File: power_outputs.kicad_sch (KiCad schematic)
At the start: 10 parts, among them Q1 BSS138, Q3 MMBT3904, Q4 MMBT3906

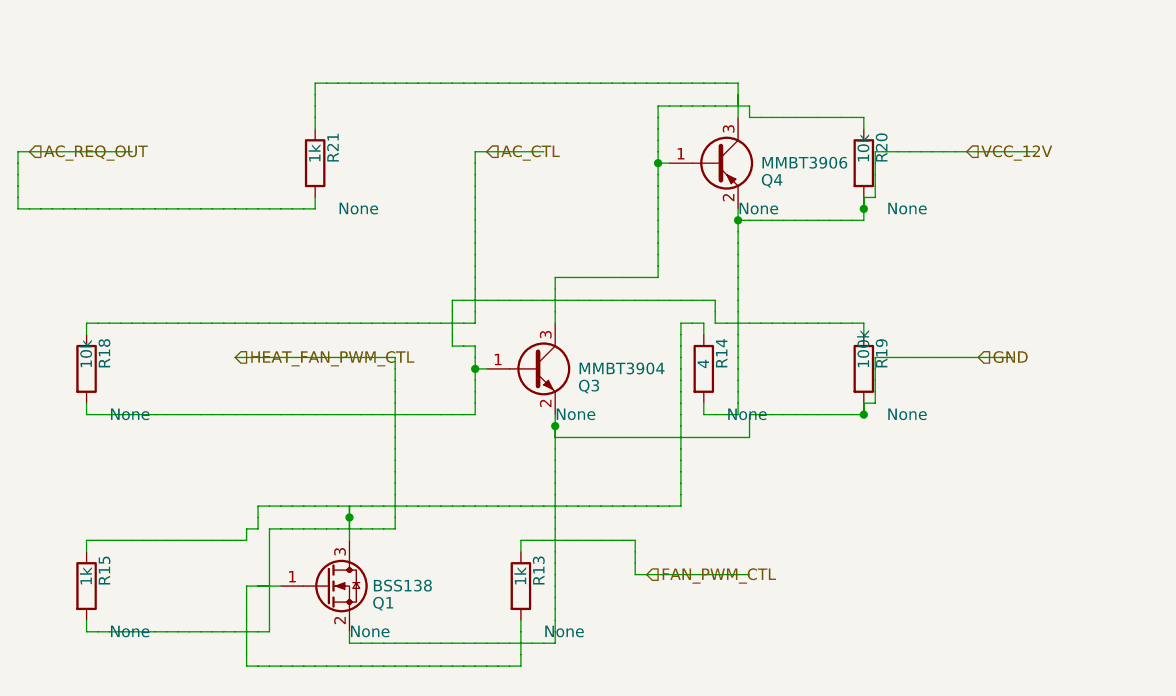
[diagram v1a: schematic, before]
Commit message: fix router map cell no more mark for pins
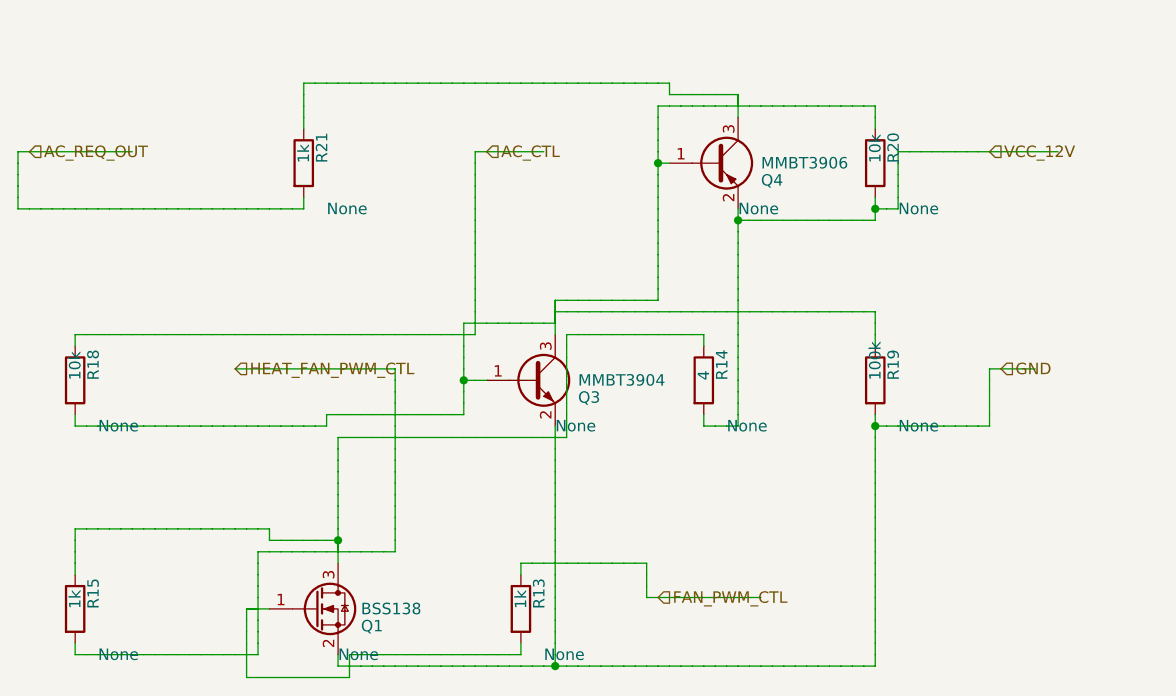
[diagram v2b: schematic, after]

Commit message: рефакторинг проекта и начала прогона тестов
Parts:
- R14: value 4 -> 4.7k

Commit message: fix writer
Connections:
- net AC_CTL: no longer Q1.1 (G), Q1.2 (S), Q1.3 (D), Q3.1 (B), Q3.2 (E), Q3.3 (C), Q4.1 (B), Q4.2 (E), Q4.3 (C), R13.1, R13.2, R14.1, R14.2, R15.1, R15.2, R18.2, R19.1, R19.2, R20.1, R20.2, R21.1
- new net: Q1.3 (D), R14.1, R15.1
- new net: Q3.1 (B), Q3.3 (C), Q4.1 (B), R18.2, R19.1, R20.1
- new net: Q4.3 (C), R21.1
- new net: Q1.1 (G), R13.2
- new net FAN_PWM_CTL: R13.1
- new net GND: Q1.2 (S), Q3.2 (E), R19.2
- new net HEAT_FAN_PWM_CTL: R15.2
- new net VCC_12V: Q4.2 (E), R14.2, R20.2

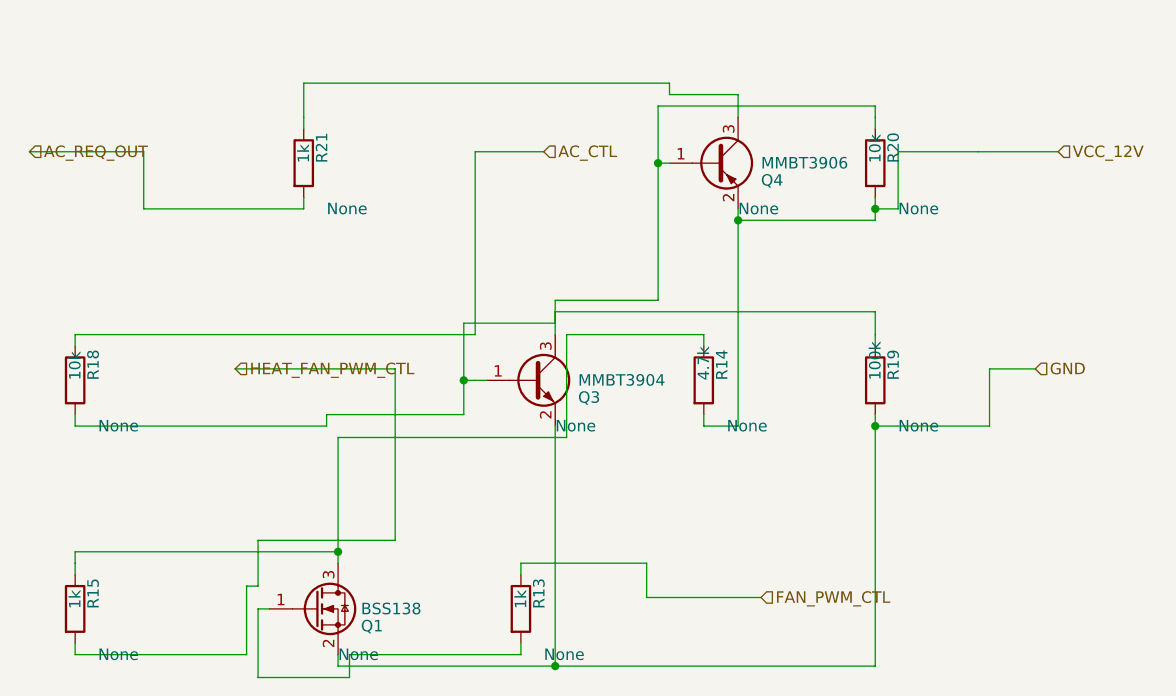
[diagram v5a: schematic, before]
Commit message: реализована 2я занятость клетки
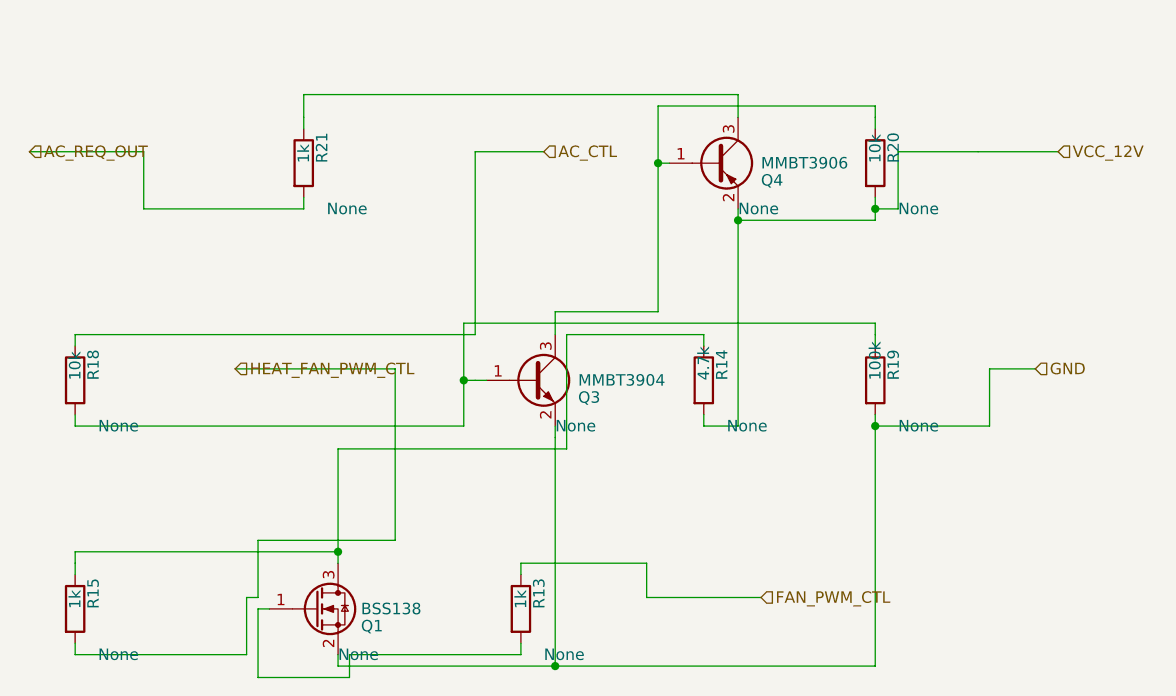
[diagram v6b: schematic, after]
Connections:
- net at Q3.1 (B), R18.2, R19.1: no longer Q3.3 (C), Q4.1 (B), R20.1
- new net: Q3.3 (C), Q4.1 (B), R20.1
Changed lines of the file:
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@@
 		(instances
 			(project "Untitled"
-				(path "/2bec01fa-02fa-473d-b0ad-ed352eecf5c4"
+				(path "/d529702e-f007-4e27-8b1f-a583131970cf"
 					(reference "Q1")
 					(unit 1)
@@
 		(instances
 			(project "Untitled"
-				(path "/2bec01fa-02fa-473d-b0ad-ed352eecf5c4"
+				(path "/d529702e-f007-4e27-8b1f-a583131970cf"
 					(reference "Q3")
 					(unit 1)
@@
 		(instances
 			(project "Untitled"
-				(path "/2bec01fa-02fa-473d-b0ad-ed352eecf5c4"
+				(path "/d529702e-f007-4e27-8b1f-a583131970cf"
 					(reference "Q4")
 					(unit 1)
@@
 		(instances
 			(project "Untitled"
-				(path "/2bec01fa-02fa-473d-b0ad-ed352eecf5c4"
+				(path "/d529702e-f007-4e27-8b1f-a583131970cf"
 					(reference "R13")
 					(unit 1)
@@
 		(instances
 			(project "Untitled"
-				(path "/2bec01fa-02fa-473d-b0ad-ed352eecf5c4"
+				(path "/d529702e-f007-4e27-8b1f-a583131970cf"
 					(reference "R14")
 					(unit 1)
@@
 		(instances
 			(project "Untitled"
-				(path "/2bec01fa-02fa-473d-b0ad-ed352eecf5c4"
+				(path "/d529702e-f007-4e27-8b1f-a583131970cf"
 					(reference "R15")
 					(unit 1)
@@
 		(instances
 			(project "Untitled"
-				(path "/2bec01fa-02fa-473d-b0ad-ed352eecf5c4"
+				(path "/d529702e-f007-4e27-8b1f-a583131970cf"
 					(reference "R18")
 					(unit 1)
@@
 		(instances
 			(project "Untitled"
-				(path "/2bec01fa-02fa-473d-b0ad-ed352eecf5c4"
+				(path "/d529702e-f007-4e27-8b1f-a583131970cf"
 					(reference "R19")
 					(unit 1)
@@
 		(instances
 			(project "Untitled"
-				(path "/2bec01fa-02fa-473d-b0ad-ed352eecf5c4"
+				(path "/d529702e-f007-4e27-8b1f-a583131970cf"
 					(reference "R20")
 					(unit 1)
@@
 		(instances
 			(project "Untitled"
-				(path "/2bec01fa-02fa-473d-b0ad-ed352eecf5c4"
+				(path "/d529702e-f007-4e27-8b1f-a583131970cf"
 					(reference "R21")
 					(unit 1)
@@
 	(wire
 		(pts
-			(xy 63.5 27.94) (xy 63.5 39.37)
-		)
-		(stroke
-			(width 0)
-			(type default)
-		)
-	)
-	(wire
-		(pts
-			(xy 63.5 39.37) (xy 38.1 39.37)
-		)
-		(stroke
-			(width 0)
-			(type default)
-		)
-	)
-	(wire
-		(pts
-			(xy 38.1 39.37) (xy 38.1 52.07)
+			(xy 63.5 27.94) (xy 63.5 40.64)
+		)
+		(stroke
+			(width 0)
+			(type default)
+		)
+	)
+	(wire
+		(pts
+			(xy 63.5 40.64) (xy 38.1 40.64)
+		)
+		(stroke
+			(width 0)
+			(type default)
+		)
+	)
+	(wire
+		(pts
+			(xy 38.1 40.64) (xy 38.1 52.07)
 		)
 		(stroke
@@
 	(wire
 		(pts
-			(xy 52.07 26.67) (xy 62.23 26.67)
-		)
-		(stroke
-			(width 0)
-			(type default)
-		)
-	)
-	(wire
-		(pts
-			(xy 62.23 26.67) (xy 62.23 25.4)
-		)
-		(stroke
-			(width 0)
-			(type default)
-		)
-	)
-	(wire
-		(pts
-			(xy 62.23 25.4) (xy 97.79 25.4)
-		)
-		(stroke
-			(width 0)
-			(type default)
-		)
-	)
-	(wire
-		(pts
-			(xy 97.79 25.4) (xy 97.79 27.94)
+			(xy 52.07 26.67) (xy 97.79 26.67)
+		)
+		(stroke
+			(width 0)
+			(type default)
+		)
+	)
+	(wire
+		(pts
+			(xy 97.79 26.67) (xy 97.79 27.94)
 		)
 		(stroke
@@
 	(wire
 		(pts
-			(xy 8.89 38.1) (xy 36.83 38.1)
-		)
-		(stroke
-			(width 0)
-			(type default)
-		)
-	)
-	(wire
-		(pts
-			(xy 36.83 38.1) (xy 36.83 36.83)
-		)
-		(stroke
-			(width 0)
-			(type default)
-		)
-	)
-	(wire
-		(pts
-			(xy 36.83 36.83) (xy 52.07 36.83)
-		)
-		(stroke
-			(width 0)
-			(type default)
-		)
-	)
-	(wire
-		(pts
-			(xy 52.07 36.83) (xy 52.07 33.02)
+			(xy 8.89 38.1) (xy 52.07 38.1)
+		)
+		(stroke
+			(width 0)
+			(type default)
+		)
+	)
+	(wire
+		(pts
+			(xy 52.07 38.1) (xy 52.07 33.02)
 		)
 		(stroke
@@
 	(wire
 		(pts
-			(xy 62.23 27.94) (xy 62.23 24.13)
-		)
-		(stroke
-			(width 0)
-			(type default)
-		)
-	)
-	(wire
-		(pts
-			(xy 62.23 24.13) (xy 73.66 24.13)
-		)
-		(stroke
-			(width 0)
-			(type default)
-		)
-	)
-	(wire
-		(pts
-			(xy 73.66 24.13) (xy 73.66 8.89)
+			(xy 62.23 27.94) (xy 62.23 25.4)
+		)
+		(stroke
+			(width 0)
+			(type default)
+		)
+	)
+	(wire
+		(pts
+			(xy 62.23 25.4) (xy 73.66 25.4)
+		)
+		(stroke
+			(width 0)
+			(type default)
+		)
+	)
+	(wire
+		(pts
+			(xy 73.66 25.4) (xy 73.66 8.89)
 		)
 		(stroke
@@
 	(wire
 		(pts
-			(xy 82.55 1.27) (xy 74.93 1.27)
-		)
-		(stroke
-			(width 0)
-			(type default)
-		)
-	)
-	(wire
-		(pts
-			(xy 74.93 1.27) (xy 74.93 0)
-		)
-		(stroke
-			(width 0)
-			(type default)
-		)
-	)
-	(wire
-		(pts
-			(xy 74.93 0) (xy 34.29 0)
-		)
-		(stroke
-			(width 0)
-			(type default)
-		)
-	)
-	(wire
-		(pts
-			(xy 34.29 0) (xy 34.29 3.81)
+			(xy 82.55 1.27) (xy 34.29 1.27)
+		)
+		(stroke
+			(width 0)
+			(type default)
+		)
+	)
+	(wire
+		(pts
+			(xy 34.29 1.27) (xy 34.29 3.81)
 		)
 		(stroke
@@
 	(wire
 		(pts
-			(xy 27.94 63.5) (xy 27.94 55.88)
-		)
-		(stroke
-			(width 0)
-			(type default)
-		)
-	)
-	(wire
-		(pts
-			(xy 27.94 55.88) (xy 29.21 55.88)
-		)
-		(stroke
-			(width 0)
-			(type default)
-		)
-	)
-	(wire
-		(pts
-			(xy 29.21 55.88) (xy 29.21 50.8)
-		)
-		(stroke
+			(xy 27.94 63.5) (xy 27.94 57.15)
+		)
+		(stroke
+			(width 0)
+			(type default)
+		)
+	)
+	(wire
+		(pts
+			(xy 27.94 57.15) (xy 29.21 57.15)
+		)
+		(stroke
+			(width 0)
+			(type default)
+		)
+	)
+	(wire
+		(pts
+			(xy 29.21 57.15) (xy 29.21 50.8)
+		)
+		(stroke

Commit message: fic placer for small schemes
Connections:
- net AC_BASE: now reaches Q3.1 (B), R18.2, R19.1
- net AC_PNP_BASE: now reaches Q3.3 (C), Q4.1 (B), R20.1
- net FAN_GATE: now reaches Q1.1 (G), R13.2
- net FAN_PWM_NODE: now reaches Q1.3 (D), R14.1, R15.1
- net AC_REQ: now reaches Q4.3 (C), R21.1
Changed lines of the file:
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@@
 		(instances
 			(project "Untitled"
-				(path "/445c904c-f531-4f41-953b-9ab8c092722a"
+				(path "/bd3444a0-416b-43f5-847d-17557aca00e5"
 					(reference "Q1")
 					(unit 1)
@@
 		(instances
 			(project "Untitled"
-				(path "/445c904c-f531-4f41-953b-9ab8c092722a"
+				(path "/bd3444a0-416b-43f5-847d-17557aca00e5"
 					(reference "Q3")
 					(unit 1)
@@
 		(instances
 			(project "Untitled"
-				(path "/445c904c-f531-4f41-953b-9ab8c092722a"
+				(path "/bd3444a0-416b-43f5-847d-17557aca00e5"
 					(reference "Q4")
 					(unit 1)
@@
 		(instances
 			(project "Untitled"
-				(path "/445c904c-f531-4f41-953b-9ab8c092722a"
+				(path "/bd3444a0-416b-43f5-847d-17557aca00e5"
 					(reference "R13")
 					(unit 1)
@@
 		(instances
 			(project "Untitled"
-				(path "/445c904c-f531-4f41-953b-9ab8c092722a"
+				(path "/bd3444a0-416b-43f5-847d-17557aca00e5"
 					(reference "R14")
 					(unit 1)
@@
 		(instances
 			(project "Untitled"
-				(path "/445c904c-f531-4f41-953b-9ab8c092722a"
+				(path "/bd3444a0-416b-43f5-847d-17557aca00e5"
 					(reference "R15")
 					(unit 1)
@@
 		(instances
 			(project "Untitled"
-				(path "/445c904c-f531-4f41-953b-9ab8c092722a"
+				(path "/bd3444a0-416b-43f5-847d-17557aca00e5"
 					(reference "R18")
 					(unit 1)
@@
 		(instances
 			(project "Untitled"
-				(path "/445c904c-f531-4f41-953b-9ab8c092722a"
+				(path "/bd3444a0-416b-43f5-847d-17557aca00e5"
 					(reference "R19")
 					(unit 1)
@@
 		(instances
 			(project "Untitled"
-				(path "/445c904c-f531-4f41-953b-9ab8c092722a"
+				(path "/bd3444a0-416b-43f5-847d-17557aca00e5"
 					(reference "R20")
 					(unit 1)
@@
 		(instances
 			(project "Untitled"
-				(path "/445c904c-f531-4f41-953b-9ab8c092722a"
+				(path "/bd3444a0-416b-43f5-847d-17557aca00e5"
 					(reference "R21")
 					(unit 1)
@@
 		(color 0 0 0 0)
 	)
+	(label "FAN_GATE"
+		(at 49.53 63.5 270)
+		(effects
+			(font
+				(size 1.27 1.27)
+			)
+			(justify left bottom)
+		)
+	)
+	(label "FAN_PWM_NODE"
+		(at 71.12 27.94 90)
+		(effects
+			(font
+				(size 1.27 1.27)
+			)
+			(justify left bottom)
+		)
+	)
+	(label "AC_BASE"
+		(at 53.34 33.02 180)
+		(effects
+			(font
+				(size 1.27 1.27)
+			)
+			(justify left bottom)
+		)
+	)
+	(label "AC_PNP_BASE"
+		(at 73.66 6.35 180)
+		(effects
+			(font
+				(size 1.27 1.27)
+			)
+			(justify left bottom)
+		)
+	)
+	(label "AC_REQ"
+		(at 58.42 1.27 90)
+		(effects
+			(font
+				(size 1.27 1.27)
+			)
+			(justify left bottom)
+		)
+	)
 	(hierarchical_label "VCC_12V"
